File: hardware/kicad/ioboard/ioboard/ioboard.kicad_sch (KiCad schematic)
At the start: 0 parts

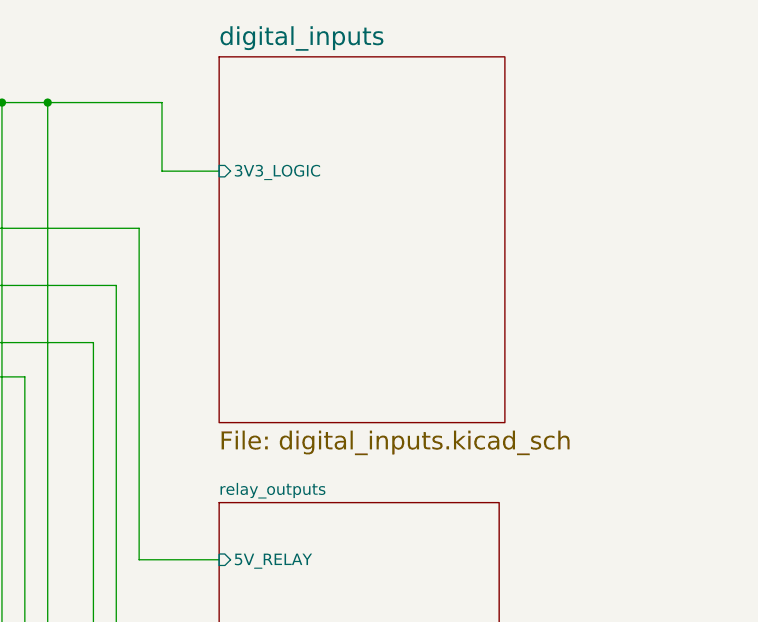
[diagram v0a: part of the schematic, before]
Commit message: docs: add Ethernet (W5500) subsystem plan, lock front end/magnetics/LED design
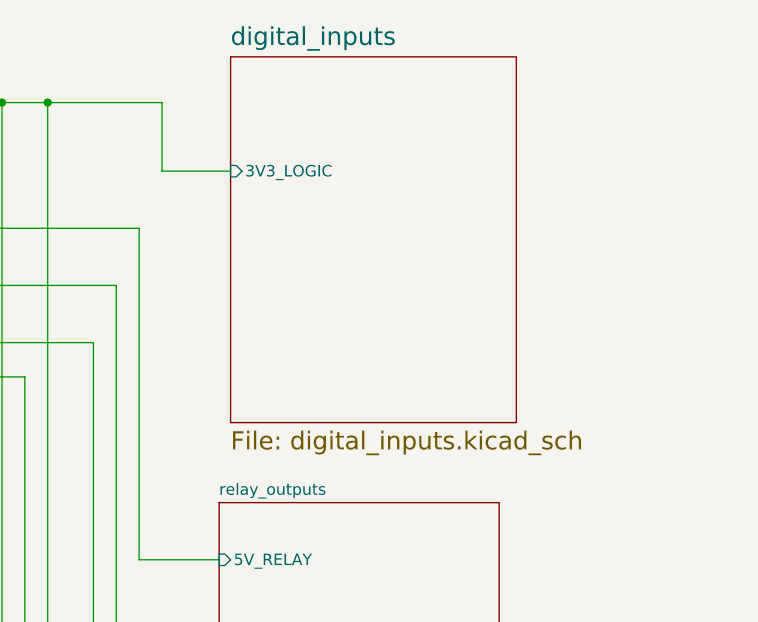
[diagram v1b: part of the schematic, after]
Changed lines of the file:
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@@
 	(wire
 		(pts
-			(xy 96.52 45.72) (xy 102.87 45.72)
+			(xy 96.52 45.72) (xy 104.14 45.72)
 		)
 		(stroke
@@
 	)
 	(sheet
-		(at 102.87 33.02)
+		(at 104.14 33.02)
 		(size 31.75 40.64)
 		(exclude_from_sim no)
@@
 		)
 		(property "Sheetname" "digital_inputs"
-			(at 102.87 31.9434 0)
+			(at 104.14 31.9434 0)
 			(effects
 				(font
@@
 		)
 		(property "Sheetfile" "digital_inputs.kicad_sch"
-			(at 102.87 74.5366 0)
+			(at 104.14 74.5366 0)
 			(effects
 				(font
@@
 		)
 		(pin "3V3_LOGIC" input
-			(at 102.87 45.72 180)
-			(effects
-				(font
+			(at 104.14 45.72 180)
+			(effects
+				(font
